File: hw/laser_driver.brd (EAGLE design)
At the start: 38.1 x 12.7 mm, 10 parts, among them IC1 895-FT232RL, IC2 998-MIC5209-3.0YM, X1 798-ZX62RD-AB-5P8

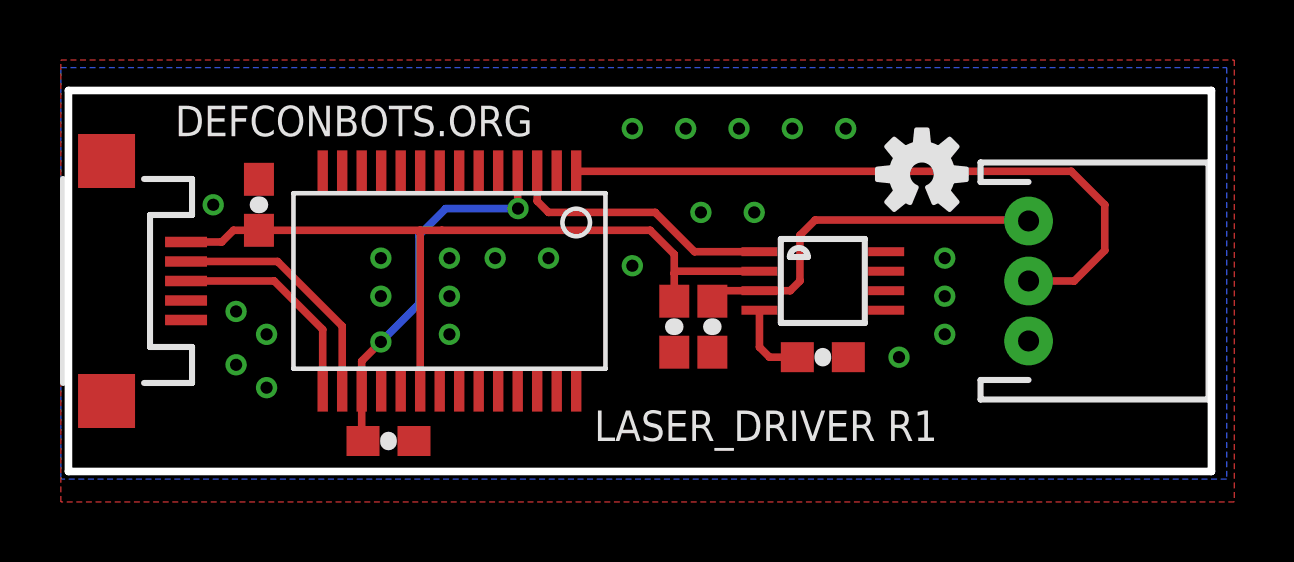
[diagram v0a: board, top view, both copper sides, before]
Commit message: Change connector to terminal block
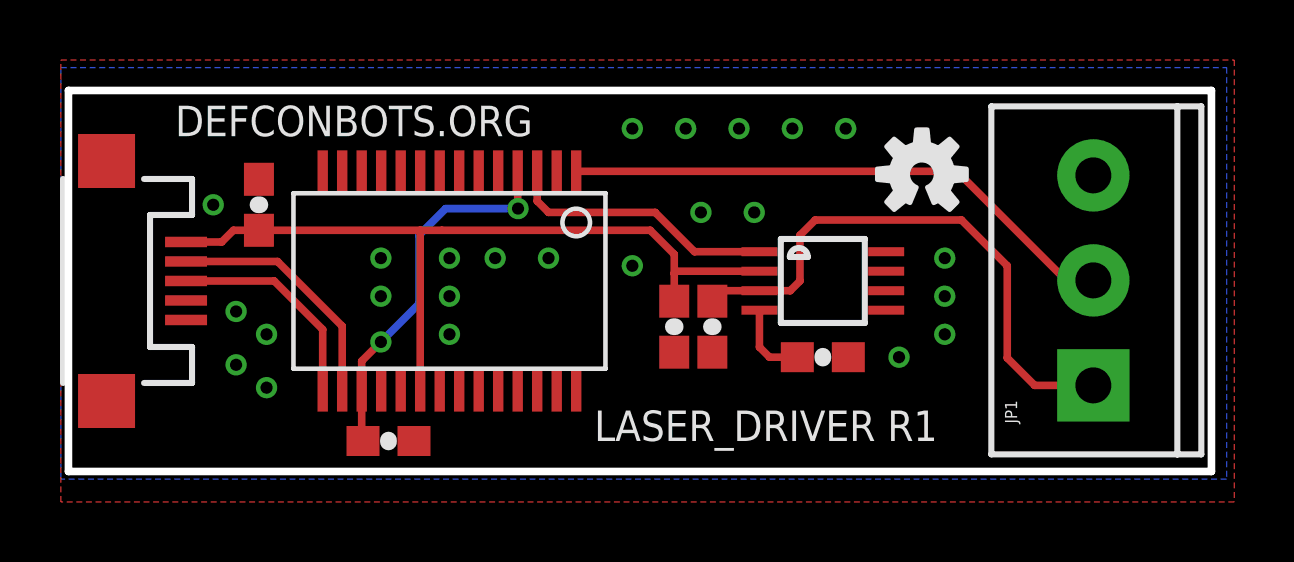
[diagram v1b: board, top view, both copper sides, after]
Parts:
- JP1: value (none) -> 651-5442251; device SparkFun-Connectors:JST-3-PTH -> SparkFun-Connectors:SCREWTERMINAL-3.5MM-3
- moved JP1 4.10 mm to (34.2, 2.87), turned to 90 degrees
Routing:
- net +3V: track 12.6 -> 18.8 mm
- net TXD: track 22.6 -> 18.7 mm
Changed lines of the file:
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@@
 <setting verticaltext="up"/>
 </settings>
-<grid distance="0.01" unitdist="inch" unit="inch" style="lines" multiple="1" display="yes" altdistance="0.005" altunitdist="inch" altunit="inch"/>
+<grid distance="0.05" unitdist="inch" unit="inch" style="lines" multiple="1" display="yes" altdistance="0.001" altunitdist="inch" altunit="inch"/>
 <layers>
 <layer number="1" name="Top" color="4" fill="1" visible="yes" active="yes"/>
@@
 <attribute name="VALUE" x="16.51" y="6.35" size="0.4064" layer="27" rot="R180"/>
 </element>
-<element name="JP1" library="SparkFun-Connectors" package="JST-3-PTH" value="" x="32.004" y="6.35" smashed="yes" rot="R270">
-<attribute name="SKU" value="PRT-09915" x="32.004" y="6.35" size="1.778" layer="27" rot="R270" display="off"/>
-<attribute name="VALUE" x="35.974" y="7.62" size="0.4064" layer="27" rot="R270"/>
-</element>
 <element name="C3" library="SparkFun-Passives" package="0603-CAP" value="C1608X5R1C106M080AB" x="20.193" y="4.826" smashed="yes" rot="R270">
 <attribute name="VALUE" x="19.05" y="5.842" size="0.4064" layer="27" font="vector" rot="R270"/>
@@
 </element>
 <element name="LOGO1" library="SparkFun-Aesthetics" package="OSHW-LOGO-S" value="OSHW-LOGOS" x="28.448" y="9.906"/>
+<element name="JP1" library="SparkFun-Connectors" package="SCREWTERMINAL-3.5MM-3" value="651-5442251" x="34.163" y="2.8702" rot="R90"/>
 </elements>
 <signals>
@@
 <contactref element="C6" pad="2"/>
 <contactref element="C4" pad="2"/>
-<contactref element="JP1" pad="3"/>
 <polygon width="0.254" layer="1">
 <vertex x="-0.254" y="13.716"/>
@@
 <via x="14.224" y="7.112" extent="1-16" drill="0.4064"/>
 <via x="16.002" y="7.112" extent="1-16" drill="0.4064"/>
+<contactref element="JP1" pad="3"/>
 <wire x1="12.375" y1="2.694" x2="10.425" y2="2.694" width="0" layer="19" extent="1-1"/>
 </signal>
@@
 <signal name="TXD">
 <contactref element="IC1" pad="1"/>
+<wire x1="16.925" y1="10.006" x2="29.618" y2="10.006" width="0.254" layer="1"/>
 <contactref element="JP1" pad="2"/>
-<wire x1="33.428" y1="10.006" x2="34.544" y2="8.89" width="0.254" layer="1"/>
-<wire x1="34.544" y1="8.89" x2="34.544" y2="7.366" width="0.254" layer="1"/>
-<wire x1="34.544" y1="7.366" x2="33.528" y2="6.35" width="0.254" layer="1"/>
-<wire x1="33.528" y1="6.35" x2="32.004" y2="6.35" width="0.254" layer="1"/>
-<wire x1="16.925" y1="10.006" x2="33.428" y2="10.006" width="0.254" layer="1"/>
+<wire x1="29.618" y1="10.006" x2="33.2538" y2="6.3702" width="0.254" layer="1"/>
+<wire x1="33.2538" y1="6.3702" x2="34.163" y2="6.3702" width="0.254" layer="1"/>
 </signal>
 <signal name="LASER_EN">
@@
 <signal name="+3V">
 <contactref element="C4" pad="1"/>
-<contactref element="JP1" pad="1"/>
 <contactref element="IC2" pad="3"/>
 <wire x1="23.0329" y1="6.0256" x2="24.0596" y2="6.0256" width="0.254" layer="1"/>
@@
 <wire x1="24.384" y1="6.35" x2="24.384" y2="7.874" width="0.254" layer="1"/>
 <wire x1="24.384" y1="7.874" x2="24.892" y2="8.382" width="0.254" layer="1"/>
-<wire x1="24.892" y1="8.382" x2="31.972" y2="8.382" width="0.254" layer="1"/>
-<wire x1="31.972" y1="8.382" x2="32.004" y2="8.35" width="0.254" layer="1"/>
+<wire x1="24.892" y1="8.382" x2="29.7688" y2="8.382" width="0.254" layer="1"/>
 <wire x1="23.0329" y1="6.0256" x2="21.8126" y2="6.0256" width="0.254" layer="1"/>
 <wire x1="21.8126" y1="6.0256" x2="21.463" y2="5.676" width="0.254" layer="1"/>
+<contactref element="JP1" pad="1"/>
+<wire x1="29.7688" y1="8.382" x2="31.2928" y2="6.858" width="0.254" layer="1"/>
+<wire x1="31.2928" y1="6.858" x2="31.2928" y2="3.7846" width="0.254" layer="1"/>
+<wire x1="31.2928" y1="3.7846" x2="32.2072" y2="2.8702" width="0.254" layer="1"/>
+<wire x1="32.2072" y1="2.8702" x2="34.163" y2="2.8702" width="0.254" layer="1"/>
 </signal>
 <signal name="N$2">

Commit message: Cleanup for fab. Add bom and gerbers.
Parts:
- moved C3 0.76 mm to (19.4, 4.83)

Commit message: Fix noise cap for the regulator
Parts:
- C6: value C1608X5R1C106M080AB -> VJ0603A471KXQPW1BC
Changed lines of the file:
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@@
 <attribute name="VALUE" x="22.606" y="3.048" size="1.27" layer="27" ratio="10"/>
 </element>
-<element name="C6" library="SparkFun-Passives" package="0603-CAP" value="C1608X5R1C106M080AB" x="25.146" y="3.81" smashed="yes">
+<element name="C6" library="SparkFun-Passives" package="0603-CAP" value="VJ0603A471KXQPW1BC" x="25.146" y="3.81" smashed="yes">
 <attribute name="VALUE" x="24.13" y="2.667" size="0.4064" layer="27" font="vector"/>
 </element>

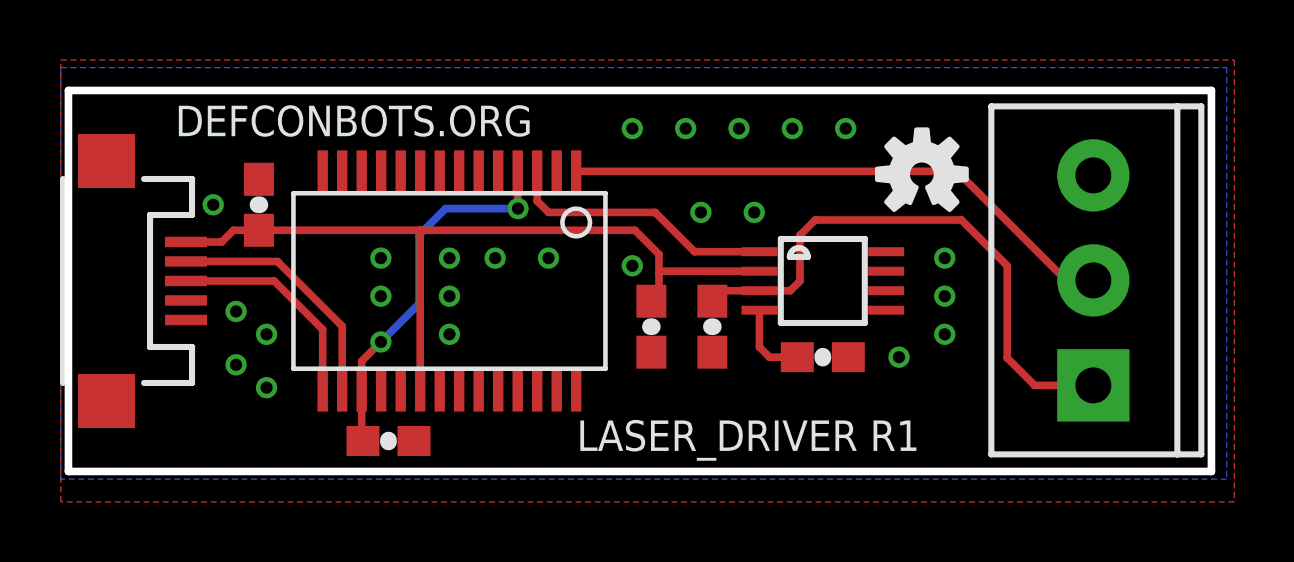
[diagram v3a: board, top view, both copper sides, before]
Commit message: Fix part numbers for regulator and usb plug. Fix disconnectoed ground pin (4) which was a really stupid mistake...
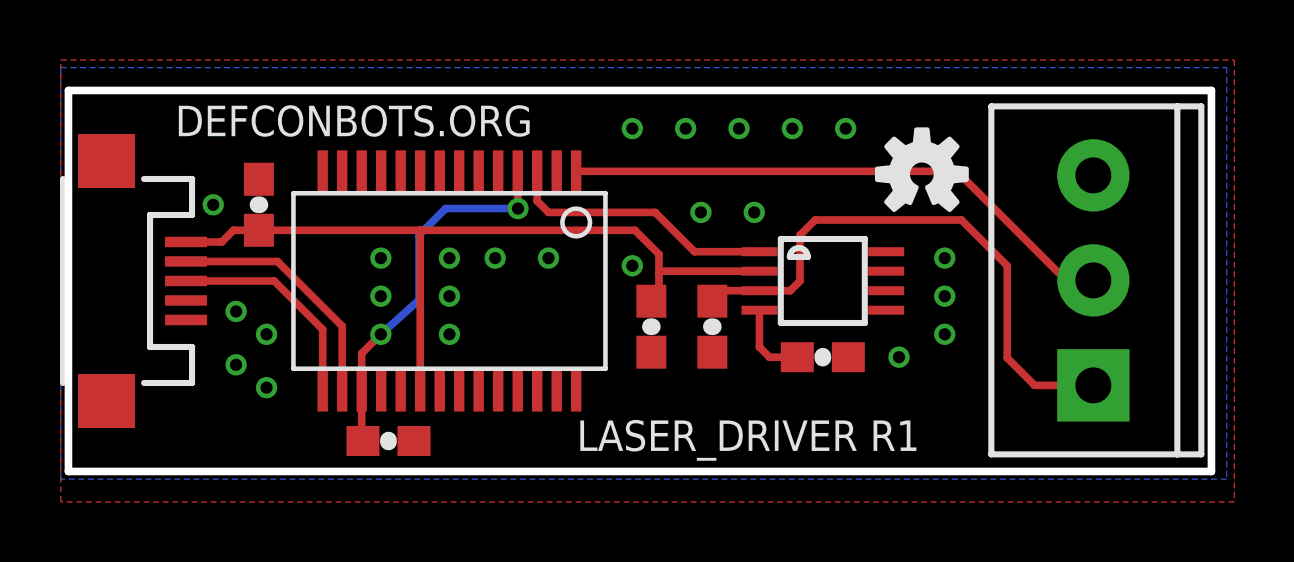
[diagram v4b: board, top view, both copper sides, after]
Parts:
- IC2: value 998-MIC5209-3.0YM -> 998-MIC5219-3.0YMM
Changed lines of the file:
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@@
 <setting verticaltext="up"/>
 </settings>
-<grid distance="2" unitdist="mil" unit="mil" style="lines" multiple="1" display="yes" altdistance="0.001" altunitdist="inch" altunit="inch"/>
+<grid distance="5" unitdist="mil" unit="mil" style="lines" multiple="1" display="yes" altdistance="0.001" altunitdist="inch" altunit="inch"/>
 <layers>
 <layer number="1" name="Top" color="4" fill="1" visible="yes" active="yes"/>
@@
 <layer number="23" name="tOrigins" color="15" fill="1" visible="yes" active="yes"/>
 <layer number="24" name="bOrigins" color="15" fill="1" visible="yes" active="yes"/>
-<layer number="25" name="tNames" color="7" fill="1" visible="yes" active="yes"/>
-<layer number="26" name="bNames" color="7" fill="1" visible="yes" active="yes"/>
+<layer number="25" name="tNames" color="7" fill="1" visible="no" active="yes"/>
+<layer number="26" name="bNames" color="7" fill="1" visible="no" active="yes"/>
 <layer number="27" name="tValues" color="7" fill="1" visible="no" active="yes"/>
 <layer number="28" name="bValues" color="7" fill="1" visible="no" active="yes"/>
-<layer number="29" name="tStop" color="7" fill="3" visible="yes" active="yes"/>
-<layer number="30" name="bStop" color="7" fill="6" visible="yes" active="yes"/>
-<layer number="31" name="tCream" color="7" fill="4" visible="yes" active="yes"/>
-<layer number="32" name="bCream" color="7" fill="5" visible="yes" active="yes"/>
+<layer number="29" name="tStop" color="7" fill="3" visible="no" active="yes"/>
+<layer number="30" name="bStop" color="7" fill="6" visible="no" active="yes"/>
+<layer number="31" name="tCream" color="7" fill="4" visible="no" active="yes"/>
+<layer number="32" name="bCream" color="7" fill="5" visible="no" active="yes"/>
 <layer number="33" name="tFinish" color="6" fill="3" visible="no" active="yes"/>
 <layer number="34" name="bFinish" color="6" fill="6" visible="no" active="yes"/>
@@
 <layer number="37" name="tTest" color="7" fill="1" visible="no" active="yes"/>
 <layer number="38" name="bTest" color="7" fill="1" visible="no" active="yes"/>
-<layer number="39" name="tKeepout" color="4" fill="11" visible="yes" active="yes"/>
-<layer number="40" name="bKeepout" color="1" fill="11" visible="yes" active="yes"/>
-<layer number="41" name="tRestrict" color="4" fill="10" visible="yes" active="yes"/>
-<layer number="42" name="bRestrict" color="1" fill="10" visible="yes" active="yes"/>
+<layer number="39" name="tKeepout" color="4" fill="11" visible="no" active="yes"/>
+<layer number="40" name="bKeepout" color="1" fill="11" visible="no" active="yes"/>
+<layer number="41" name="tRestrict" color="4" fill="10" visible="no" active="yes"/>
+<layer number="42" name="bRestrict" color="1" fill="10" visible="no" active="yes"/>
 <layer number="43" name="vRestrict" color="2" fill="10" visible="no" active="yes"/>
 <layer number="44" name="Drills" color="7" fill="1" visible="no" active="yes"/>
@@
 <layer number="114" name="Route14" color="7" fill="1" visible="no" active="no"/>
 <layer number="115" name="Route15" color="7" fill="1" visible="no" active="no"/>
-<layer number="200" name="200bmp" color="1" fill="10" visible="yes" active="yes"/>
+<layer number="200" name="200bmp" color="1" fill="10" visible="no" active="yes"/>
 <layer number="217" name="217bmp" color="18" fill="1" visible="no" active="no"/>
 <layer number="218" name="218bmp" color="19" fill="1" visible="no" active="no"/>
@@
 <attribute name="VALUE" x="20.32" y="5.842" size="0.4064" layer="27" font="vector" rot="R270"/>
 </element>
-<element name="IC2" library="v-reg-micrel" package="MSOP08" value="998-MIC5209-3.0YM" x="25.146" y="6.35" smashed="yes" rot="R270">
+<element name="IC2" library="v-reg-micrel" package="MSOP08" value="998-MIC5219-3.0YMM" x="25.146" y="6.35" smashed="yes" rot="R270">
 <attribute name="OC_NEWARK" value="76C0464" x="37.084" y="13.97" size="1.778" layer="27" rot="R270" display="off"/>
 <attribute name="MPN" value="MIC5219BMM" x="37.084" y="13.97" size="1.778" layer="27" rot="R270" display="off"/>
@@
 <via x="16.002" y="7.112" extent="1-16" drill="0.4064"/>
 <contactref element="JP1" pad="3"/>
-<wire x1="12.375" y1="2.694" x2="10.425" y2="2.694" width="0" layer="19" extent="1-1"/>
 </signal>
 <signal name="USB_D-">
@@
 <wire x1="9.818" y1="1.016" x2="9.775" y2="1.059" width="0.254" layer="1"/>
 <wire x1="9.775" y1="1.059" x2="9.775" y2="2.694" width="0.254" layer="1"/>
-<wire x1="9.775" y1="2.694" x2="9.775" y2="3.679" width="0.254" layer="1"/>
-<wire x1="9.775" y1="3.679" x2="10.414" y2="4.318" width="0.254" layer="1"/>
-<via x="10.414" y="4.318" extent="1-16" drill="0.4064"/>
-<wire x1="10.414" y1="4.318" x2="11.684" y2="5.588" width="0.254" layer="16"/>
-<wire x1="11.684" y1="5.588" x2="11.684" y2="7.874" width="0.254" layer="16"/>
+<wire x1="9.775" y1="2.694" x2="9.775" y2="3.933" width="0.254" layer="1"/>
+<wire x1="9.775" y1="3.933" x2="10.414" y2="4.572" width="0.254" layer="1"/>
+<via x="10.414" y="4.572" extent="1-16" drill="0.4064"/>
+<wire x1="10.414" y1="4.572" x2="11.684" y2="5.715" width="0.254" layer="16"/>
+<wire x1="11.684" y1="5.715" x2="11.684" y2="7.874" width="0.254" layer="16"/>
 <wire x1="11.684" y1="7.874" x2="12.573" y2="8.763" width="0.254" layer="16"/>
 <wire x1="12.573" y1="8.763" x2="14.986" y2="8.763" width="0.254" layer="16"/>
